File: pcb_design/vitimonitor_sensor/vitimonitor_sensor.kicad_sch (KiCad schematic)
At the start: 43 parts, among them J1 USB_C_Receptacle_USB2.0_14P, J2 Conn_01x10, J3 Conn_01x02, J4 Conn_01x04, J5 Pin_2x5, Q1 Si2371EDS, SW1 BOOT, SW2 RESETN, U1 ESP32-C3-WROOM-02U, U2 USBLC6-2SC6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

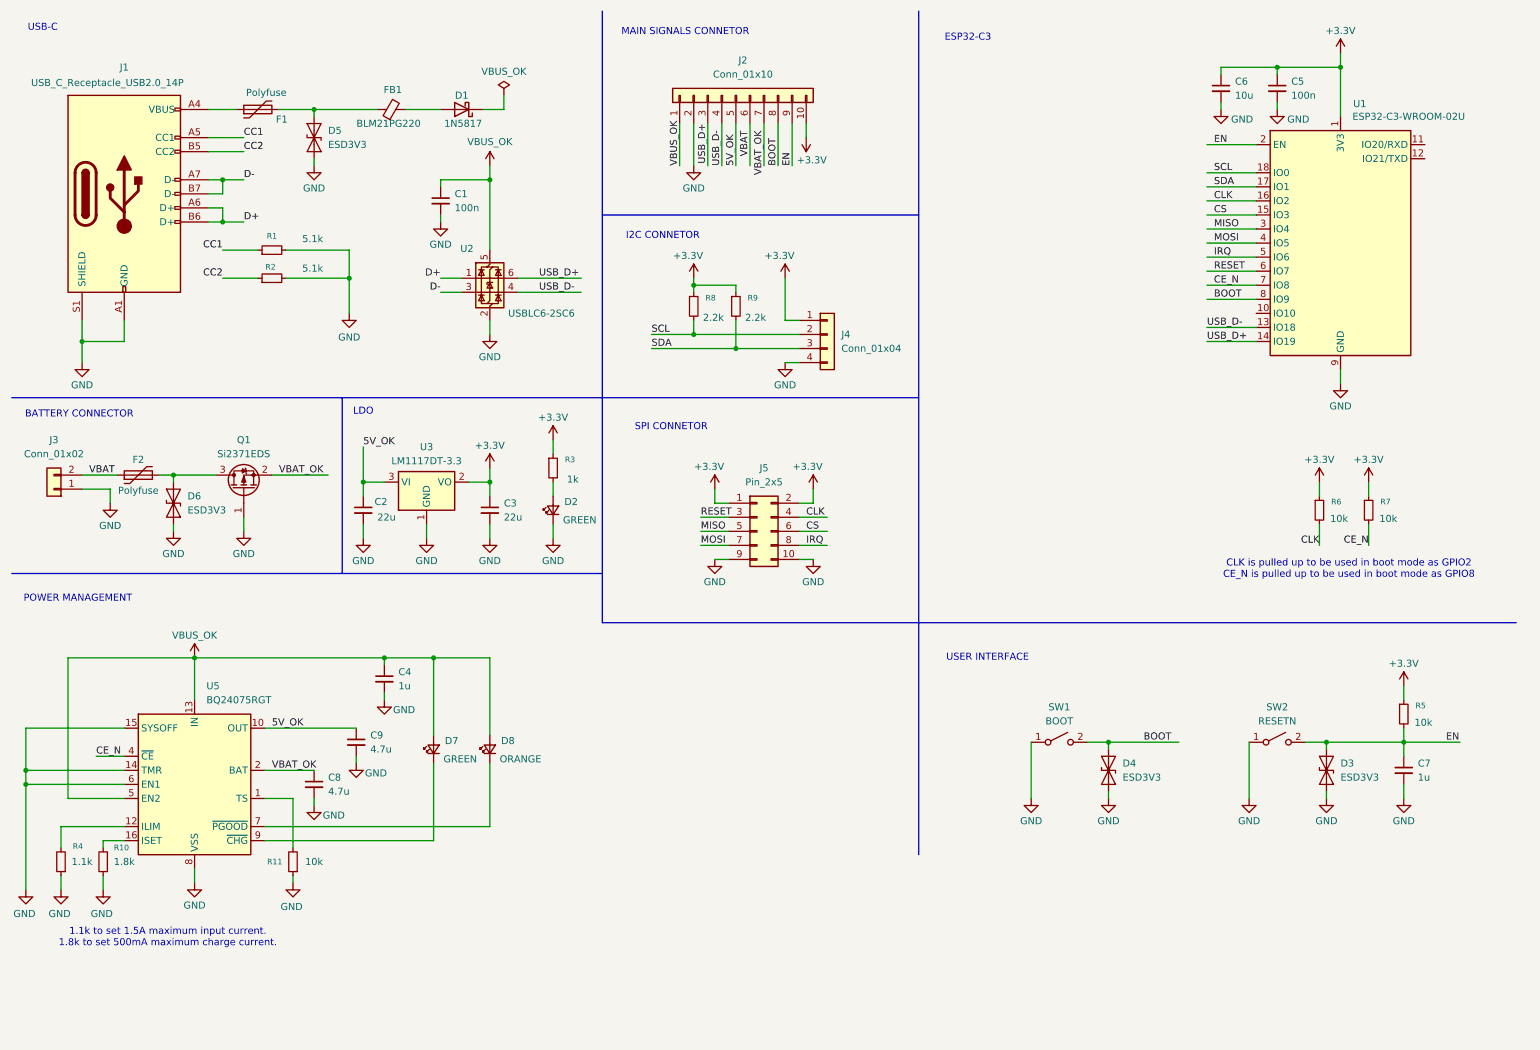
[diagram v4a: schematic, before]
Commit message: Power management completed, missiming sx1262, actual i2c sensors and uart RS485 connector
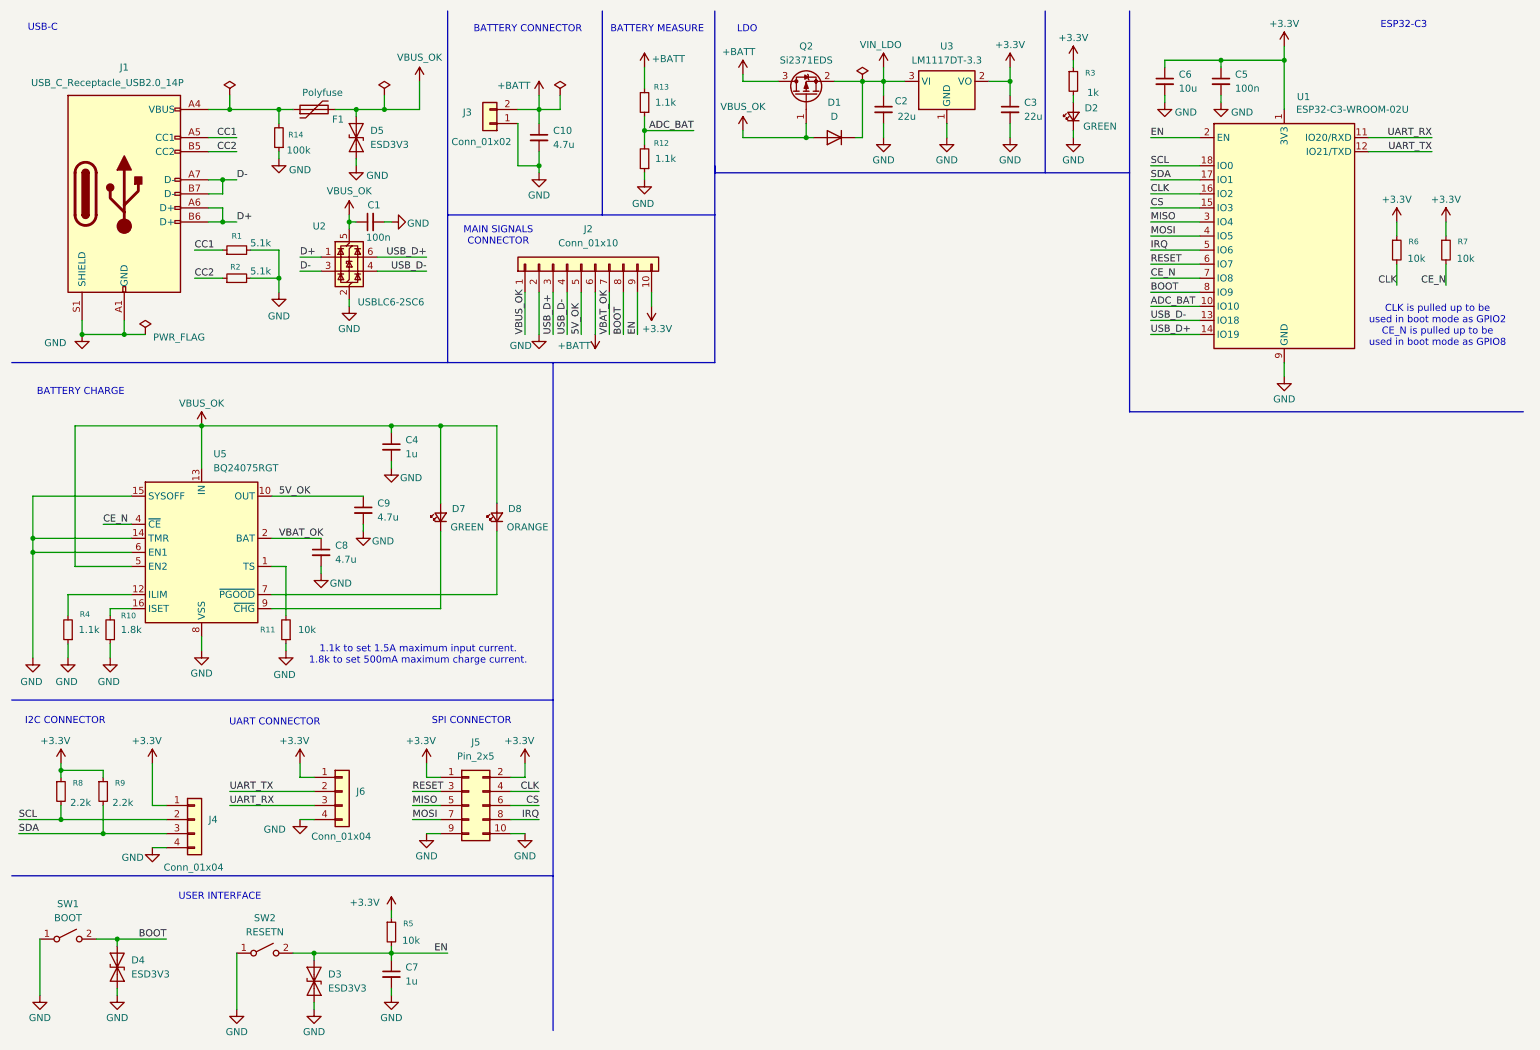
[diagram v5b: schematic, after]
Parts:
- removed D1: 1N5817, Diode_THT:D_DO-41_SOD81_P10.16mm_Horizontal, symbol Diode:1N5817
- removed D6: ESD3V3, Diode_SMD:D_SOD-923, symbol Diode:ESD9B3.3ST5G
- removed F2: Polyfuse, symbol Device:Polyfuse
- removed FB1: BLM21PG220, symbol Device:FerriteBead_Small
- removed Q1: Si2371EDS, Package_TO_SOT_SMD:SOT-23, symbol Transistor_FET:Si2371EDS
- added C10: 4.7u, symbol Device:C_Small
- added D1: D, symbol Device:D
- added J6: Conn_01x04, symbol Connector_Generic:Conn_01x04
- added Q2: Si2371EDS, Package_TO_SOT_SMD:SOT-23, symbol Transistor_FET:Si2371EDS
- added R12, R13: 1.1k, symbol Device:R_Small
- added R14: 100k, symbol Device:R_Small
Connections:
- net +3.3V: now also J6.1 (Pin_1)
- net 5V_OK: no longer C2.1, U3.3 (VI)
- net GND: now also C10.2, J6.4 (Pin_4), R12.1, R14.1
- net VBUS_OK: now also D5.2 (A2), F1.2, D1.2 (A), Q2.1 (G)
- net at F1.1, J1.A4 (VBUS), J1.A9 (VBUS)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: now also R14.2
- net ADC_BAT: now reaches U1.10 (IO10)
- net ADC_BAT: now also R12.2, R13.1
- net UART_RX: now reaches U1.11 (IO20/RXD)
- net UART_RX: now also J6.3 (Pin_3)
- net UART_TX: now reaches U1.12 (IO21/TXD)
- net UART_TX: now also J6.2 (Pin_2)
- net VBAT renamed +BATT
- net +BATT: now also C10.1, Q2.3 (D), R13.2
- new net VIN_LDO: C2.1, D1.1 (K), Q2.2 (S), U3.3 (VI)
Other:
- note added: "BATTERY CHARGE"
- note added: "BATTERY MEASURE"
- note added: "I2C CONNECTOR"
- note added: "MAIN SIGNALS CONNECTOR"
- note added: "SPI CONNECTOR"
- note added: "UART CONNECTOR"
- note removed: "I2C CONNETOR"
- note removed: "MAIN SIGNALS CONNETOR"
- note removed: "POWER MANAGEMENT"
- note removed: "SPI CONNETOR"
- moved on the sheet: C1, C2, C3, C4, C5, C6, C7, C8, C9, D2, D3, D4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

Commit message: Power management completed, missiming sx1262, actual i2c sensors and uart RS485 connector
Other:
- moved on the sheet: C7, D3, R5, SW2
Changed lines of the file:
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@@
 	(text "USER INTERFACE\n"
 		(exclude_from_sim no)
-		(at 50.292 172.72 0)
+		(at 45.974 173.736 0)
 		(effects
 			(font
@@
 	)
 	(junction
-		(at 67.31 182.88)
+		(at 68.58 181.61)
 		(diameter 0)
 		(color 0 0 0 0)
@@
 	)
 	(junction
-		(at 81.28 182.88)
+		(at 82.55 181.61)
 		(diameter 0)
 		(color 0 0 0 0)
@@
 	(wire
 		(pts
-			(xy 81.28 189.23) (xy 81.28 190.5)
+			(xy 82.55 187.96) (xy 82.55 189.23)
 		)
 		(stroke
@@
 	(wire
 		(pts
-			(xy 67.31 191.77) (xy 67.31 193.04)
+			(xy 68.58 190.5) (xy 68.58 191.77)
 		)
 		(stroke
@@
 	(wire
 		(pts
-			(xy 81.28 182.88) (xy 91.44 182.88)
+			(xy 82.55 181.61) (xy 92.71 181.61)
 		)
 		(stroke
@@
 	(wire
 		(pts
-			(xy 81.28 182.88) (xy 81.28 184.15)
+			(xy 82.55 181.61) (xy 82.55 182.88)
 		)
 		(stroke
@@
 	(wire
 		(pts
-			(xy 67.31 182.88) (xy 67.31 184.15)
+			(xy 68.58 181.61) (xy 68.58 182.88)
 		)
 		(stroke
@@
 	(wire
 		(pts
-			(xy 67.31 182.88) (xy 81.28 182.88)
+			(xy 68.58 181.61) (xy 82.55 181.61)
 		)
 		(stroke
@@
 	(wire
 		(pts
-			(xy 53.34 182.88) (xy 53.34 193.04)
+			(xy 54.61 181.61) (xy 54.61 191.77)
 		)
 		(stroke
@@
 	(wire
 		(pts
-			(xy 81.28 181.61) (xy 81.28 182.88)
+			(xy 82.55 180.34) (xy 82.55 181.61)
 		)
 		(stroke
@@
 	(wire
 		(pts
-			(xy 81.28 175.26) (xy 81.28 176.53)
+			(xy 82.55 173.99) (xy 82.55 175.26)
 		)
 		(stroke
@@
 	(wire
 		(pts
-			(xy 63.5 182.88) (xy 67.31 182.88)
+			(xy 64.77 181.61) (xy 68.58 181.61)
 		)
 		(stroke
@@
 	)
 	(label "EN"
-		(at 91.44 182.88 180)
+		(at 92.71 181.61 180)
 		(effects
 			(font
@@
 	(symbol
 		(lib_id "power:GND")
-		(at 67.31 193.04 0)
+		(at 68.58 191.77 0)
 		(unit 1)
 		(exclude_from_sim no)
@@
 		(dnp no)
 		(property "Reference" "#PWR016"
-			(at 67.31 199.39 0)
+			(at 68.58 198.12 0)
 			(effects
 				(font
@@
 		)
 		(property "Value" "GND"
-			(at 67.31 197.104 0)
+			(at 68.58 195.834 0)
 			(effects
 				(font
@@
 		)
 		(property "Footprint" ""
-			(at 67.31 193.04 0)
+			(at 68.58 191.77 0)
 			(effects
 				(font
@@
 		)
 		(property "Datasheet" ""
-			(at 67.31 193.04 0)
+			(at 68.58 191.77 0)
 			(effects
 				(font
@@
 		)
 		(property "Description" "Power symbol creates a global label with name \"GND\" , ground"
-			(at 67.31 193.04 0)
+			(at 68.58 191.77 0)
 			(effects
 				(font
@@
 	(symbol
 		(lib_id "Device:C_Small")
-		(at 81.28 186.69 0)
+		(at 82.55 185.42 0)
 		(unit 1)
 		(exclude_from_sim no)
@@
 		(fields_autoplaced yes)
 		(property "Reference" "C7"
-			(at 83.82 185.4262 0)
+			(at 85.09 184.1562 0)
 			(effects
 				(font
@@
 		)
 		(property "Value" "1u"
-			(at 83.82 187.9662 0)
+			(at 85.09 186.6962 0)
 			(effects
 				(font
@@
 		)
 		(property "Footprint" ""
-			(at 81.28 186.69 0)
+			(at 82.55 185.42 0)
 			(effects
 				(font
@@
 		)
 		(property "Datasheet" "~"
-			(at 81.28 186.69 0)
+			(at 82.55 185.42 0)
 			(effects
 				(font
@@
 		)
 		(property "Description" "Unpolarized capacitor, small symbol"
-			(at 81.28 186.69 0)
+			(at 82.55 185.42 0)
 			(effects
 				(font
@@
 	(symbol
 		(lib_id "power:GND")
-		(at 81.28 190.5 0)
+		(at 82.55 189.23 0)
 		(unit 1)
 		(exclude_from_sim no)
@@
 		(dnp no)
 		(property "Reference" "#PWR024"
-			(at 81.28 196.85 0)
+			(at 82.55 195.58 0)
 			(effects
 				(font
@@
 		)
 		(property "Value" "GND"
-			(at 81.28 194.564 0)
+			(at 82.55 193.294 0)
 			(effects
 				(font
@@
 		)
 		(property "Footprint" ""
-			(at 81.28 190.5 0)
+			(at 82.55 189.23 0)
 			(effects
 				(font
@@
 		)
 		(property "Datasheet" ""
-			(at 81.28 190.5 0)
+			(at 82.55 189.23 0)
 			(effects
 				(font
@@
 		)
 		(property "Description" "Power symbol creates a global label with name \"GND\" , ground"
-			(at 81.28 190.5 0)
+			(at 82.55 189.23 0)
 			(effects
 				(font
@@
 	(symbol
 		(lib_id "Device:R_Small")
-		(at 81.28 179.07 0)
+		(at 82.55 177.8 0)
 		(unit 1)
 		(exclude_from_sim no)
@@
 		(dnp no)
 		(property "Reference" "R5"
-			(at 84.328 177.546 0)
+			(at 85.598 176.276 0)
 			(effects
 				(font
@@
 		)
 		(property "Value" "10k"
-			(at 84.836 180.594 0)
+			(at 86.106 179.324 0)
 			(effects
 				(font
@@
 		)
 		(property "Footprint" ""
-			(at 81.28 179.07 0)
+			(at 82.55 177.8 0)
 			(effects
 				(font
@@
 		)
 		(property "Datasheet" "~"
-			(at 81.28 179.07 0)
+			(at 82.55 177.8 0)
 			(effects
 				(font
@@
 		)
 		(property "Description" "Resistor, small symbol"
-			(at 81.28 179.07 0)
+			(at 82.55 177.8 0)
 			(effects
 				(font
@@
 	(symbol
 		(lib_id "power:GND")
-		(at 53.34 193.04 0)
+		(at 54.61 191.77 0)
 		(unit 1)
 		(exclude_from_sim no)
@@
 		(dnp no)
 		(property "Reference" "#PWR022"
-			(at 53.34 199.39 0)
+			(at 54.61 198.12 0)
 			(effects
 				(font
@@
 		)
 		(property "Value" "GND"
-			(at 53.34 197.104 0)
+			(at 54.61 195.834 0)
 			(effects
 				(font
@@
 		)
 		(property "Footprint" ""
-			(at 53.34 193.04 0)
+			(at 54.61 191.77 0)
 			(effects
 				(font
@@
 		)
 		(property "Datasheet" ""
-			(at 53.34 193.04 0)
+			(at 54.61 191.77 0)
 			(effects
 				(font
@@
 		)
 		(property "Description" "Power symbol creates a global label with name \"GND\" , ground"
-			(at 53.34 193.04 0)
+			(at 54.61 191.77 0)
 			(effects
 				(font
@@
 	(symbol
 		(lib_id "power:+3.3V")
-		(at 81.28 175.26 0)
+		(at 82.55 173.99 0)
 		(unit 1)
 		(exclude_from_sim no)
@@
 		(dnp no)
 		(property "Reference" "#PWR023"
-			(at 81.28 179.07 0)
+			(at 82.55 177.8 0)
 			(effects
 				(font
@@
 		)
 		(property "Value" "+3.3V"
-			(at 76.454 173.736 0)
+			(at 77.724 172.466 0)
 			(effects
 				(font
@@
 		)
 		(property "Footprint" ""
-			(at 81.28 175.26 0)
+			(at 82.55 173.99 0)
 			(effects
 				(font
@@
 		)
 		(property "Datasheet" ""
-			(at 81.28 175.26 0)
+			(at 82.55 173.99 0)
 			(effects
 				(font
@@
 		)
 		(property "Description" "Power symbol creates a global label with name \"+3.3V\""
-			(at 81.28 175.26 0)
+			(at 82.55 173.99 0)
 			(effects
 				(font
@@
 	(symbol
 		(lib_id "Switch:SW_SPST")
-		(at 58.42 182.88 0)
+		(at 59.69 181.61 0)
 		(unit 1)
 		(exclude_from_sim no)
@@
 		(fields_autoplaced yes)
 		(property "Reference" "SW2"
-			(at 58.42 176.53 0)
+			(at 59.69 175.26 0)
 			(effects
 				(font
@@
 		)
 		(property "Value" "RESETN"
-			(at 58.42 179.07 0)
+			(at 59.69 177.8 0)
 			(effects
 				(font
@@
 		)
 		(property "Footprint" ""
-			(at 58.42 182.88 0)
+			(at 59.69 181.61 0)
 			(effects
 				(font
@@
 		)
 		(property "Datasheet" "~"
-			(at 58.42 182.88 0)
+			(at 59.69 181.61 0)
 			(effects
 				(font
@@
 		)
 		(property "Description" "Single Pole Single Throw (SPST) switch"
-			(at 58.42 182.88 0)
+			(at 59.69 181.61 0)
 			(effects
 				(font
@@
 			)
 		)
-		(property "Value" "PWR_FLAG"
-			(at 42.926 71.628 0)
+		(property "Value" "~"
+			(at 39.624 69.342 0)
 			(effects
 				(font
@@
 	(symbol
 		(lib_id "Diode:ESD9B3.3ST5G")
-		(at 67.31 187.96 90)
+		(at 68.58 186.69 90)
 		(unit 1)
 		(exclude_from_sim no)
@@
 		(fields_autoplaced yes)
 		(property "Reference" "D3"
-			(at 69.85 186.6899 90)
+			(at 71.12 185.4199 90)
 			(effects
 				(font
@@
 		)
 		(property "Value" "ESD3V3"
-			(at 69.85 189.2299 90)
+			(at 71.12 187.9599 90)
 			(effects
 				(font
@@
 		)
 		(property "Footprint" "Diode_SMD:D_SOD-923"
-			(at 67.31 187.96 0)
+			(at 68.58 186.69 0)
 			(effects
 				(font
@@
 		)
 		(property "Datasheet" "https://www.onsemi.com/pub/Collateral/ESD9B-D.PDF"
-			(at 67.31 187.96 0)
+			(at 68.58 186.69 0)
 			(effects
 				(font
@@
 		)
 		(property "Description" "ESD protection diode, 3.3Vrwm, SOD-923"
-			(at 67.31 187.96 0)
+			(at 68.58 186.69 0)
 			(effects
 				(font
